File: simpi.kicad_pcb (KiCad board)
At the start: 2 copper layers, 78 x 84 mm, 51 parts, among them J1 7111S2015X02LF_SIM_Card_Slot, J2 USB_A, J3 DIV_ANT, J4 MAIN_ANT, J5 GNSS_ANT, J6 Jack-DC, Q1 MMUN2133LT1G, Q2 MMUN2133LT1G, Q3 MMUN2133LT1G, SW1 PWR_SW, U1 strawberry_linux_TPS63070_mod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, U2 SIM7500A, U3 NanoPiNEO, U4 Adafruit_2465_Powerboost1000C

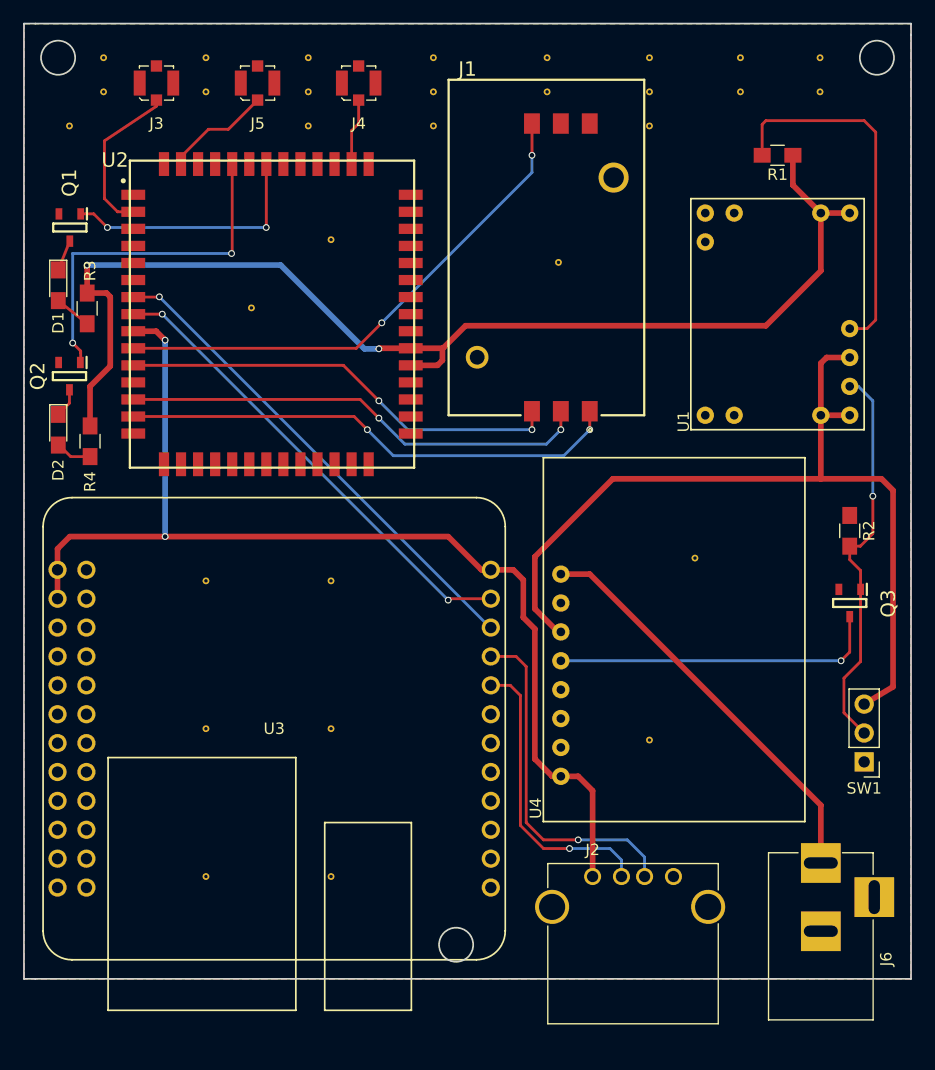
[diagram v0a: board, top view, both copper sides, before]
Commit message: Adjusted mobule footprints
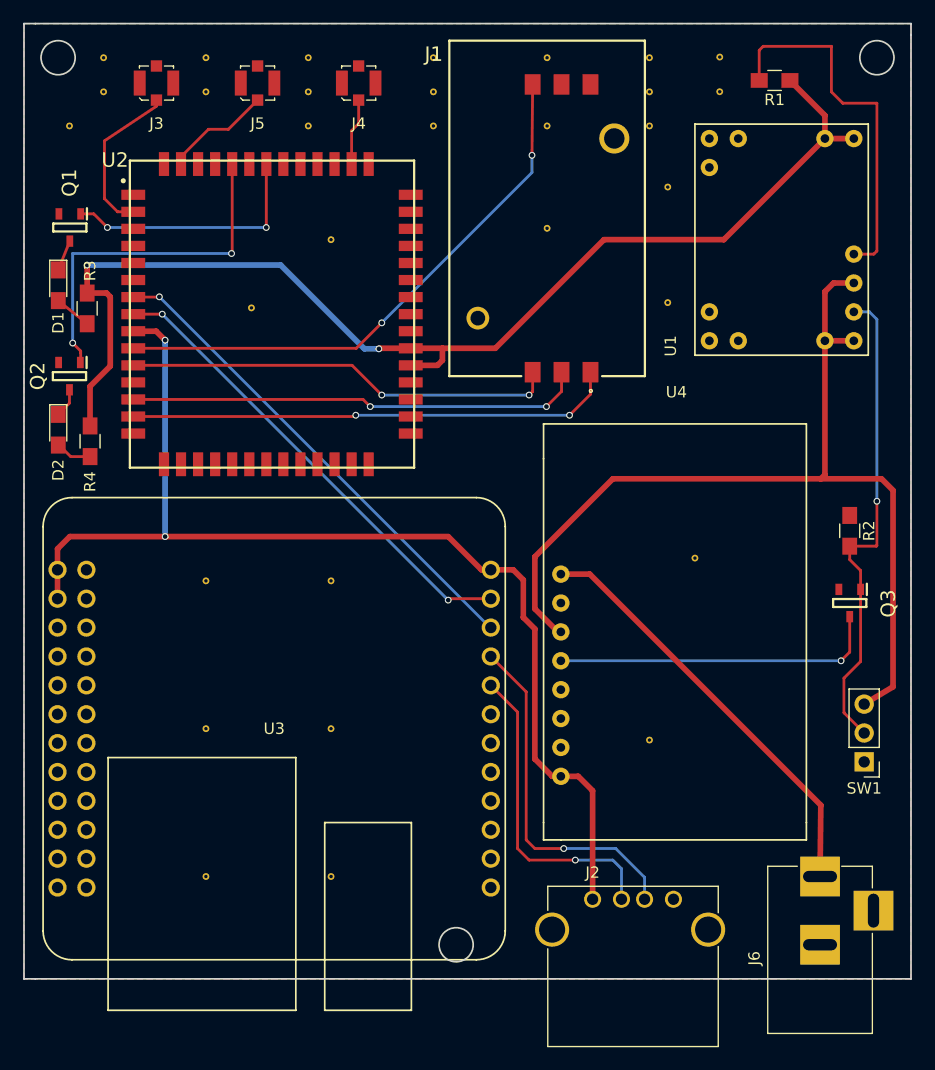
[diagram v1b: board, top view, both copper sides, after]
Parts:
- moved ? 22.9 mm to (165.6, 81.5)
- moved ? 17.6 mm to (165.6, 71.4)
- moved R1 6.59 mm to (175.0, 62.0)
- moved U1 6.56 mm to (168.0, 76.0)
- moved J1 3.44 mm to (155.0, 88.0)
- moved ? 3.16 mm to (155.0, 75.0)
- moved ? 3.00 mm to (155.0, 66.0)
- moved J2 2.00 mm to (159.0, 134.0)
- moved ? 1.82 mm to (170.2, 59.9)
- moved ? 1.82 mm to (170.2, 63.0)
- moved J6 1.19 mm to (179.0, 132.0)
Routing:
- net Net-(Q3-Pad1): track 34.9 -> 43.5 mm
- net VBAT: track 78.1 -> 84.7 mm
- net Net-(J1-Pad6): track 45.8 -> 49.2 mm
- net +5V: track 97.7 -> 99.7 mm
- net Net-(J2-Pad2): track 26.0 -> 27.9 mm
- net Net-(J1-Pad2): track 41.4 -> 40.2 mm
- net /VBUS: track 36.4 -> 37.5 mm
- net Net-(J1-Pad1): track 44.1 -> 43.0 mm
- net Net-(J1-Pad3): track 39.0 -> 38.0 mm
- net Net-(J2-Pad3): track 30.6 -> 31.1 mm

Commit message: add Q4 for logic inversion
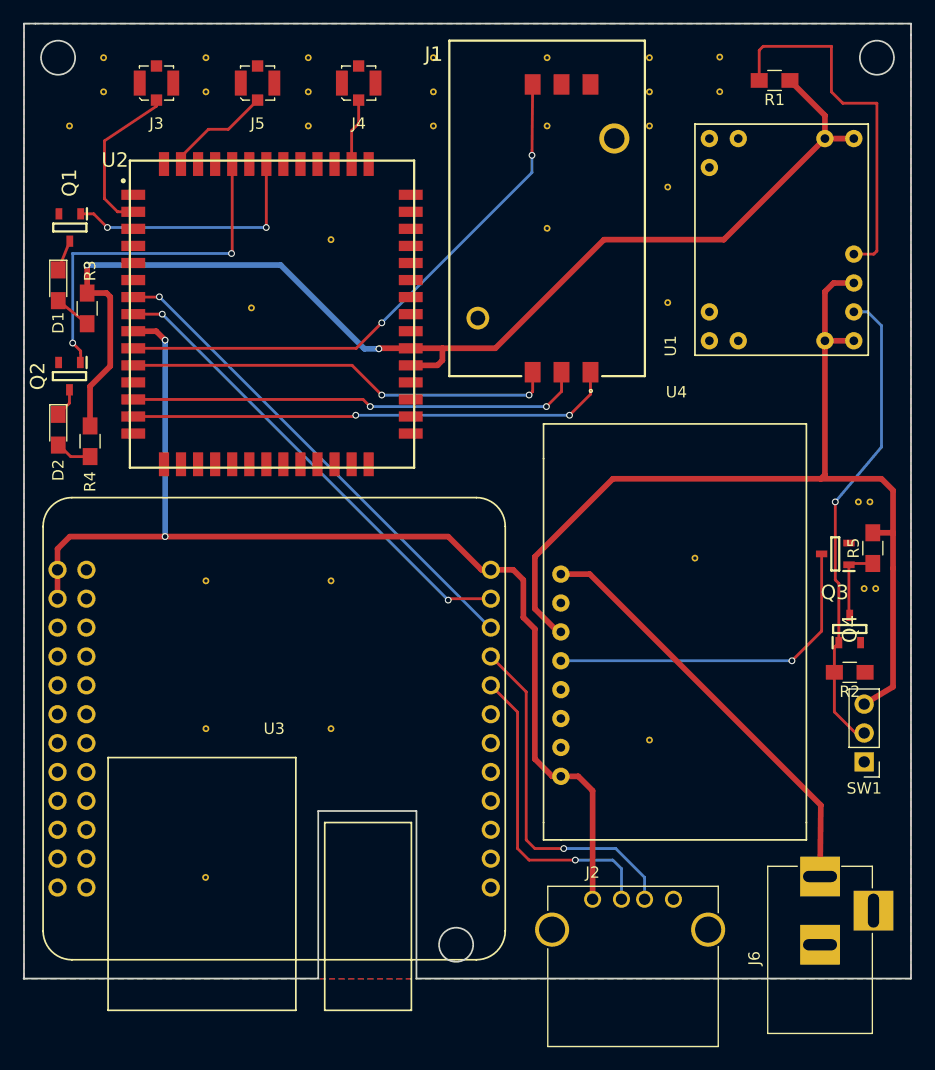
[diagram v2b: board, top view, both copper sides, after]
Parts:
- removed the ? at (136.0, 132.0)
- added ?: , mylib:via, F.Cu at (182.9, 106.7)
- added ?: , mylib:via, F.Cu at (183.9, 106.7)
- added ?: , mylib:via, F.Cu at (182.4, 99.1)
- added ?: , mylib:via, F.Cu at (183.4, 99.1)
- added Q4: MMUN2233LT1G, MMUN2133LT1G:SOT96P237X111-3N, F.Cu at (181.6, 110.2)
- added R5: 10K, Resistors_SMD:R_0805_HandSoldering, F.Cu at (183.6, 103.1)
- Q1, Q2, Q3: value MMUN2133LT1G -> MMUN2233LT1G
- moved R2 12.4 mm to (181.6, 114.0), turned to 180 degrees
- moved Q3 4.50 mm to (180.3, 103.6), turned to 180 degrees
- moved ? 0.09 mm to (125.0, 132.1)
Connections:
- R2 pad 2: Net-(Q3-Pad1) -> Net-(Q4-Pad1)
- SW1 pad 2: Net-(Q3-Pad1) -> Net-(Q4-Pad1)
- U1 pad 3: Net-(Q3-Pad1) -> Net-(Q4-Pad1)
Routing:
- net Net-(Q4-Pad1): track 0.00 -> 42.8 mm, vias 0 -> 1
- net Net-(Q3-Pad1): track 43.5 -> 6.63 mm, vias 1 -> 0
- net Net-(Q3-Pad3): track 28.8 -> 30.8 mm
- net VBAT: track 84.7 -> 86.6 mm
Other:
- outline, holes or cut-outs redrawn
